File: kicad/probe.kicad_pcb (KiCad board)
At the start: 2 copper layers, 22 parts, among them IC1 ATTINY85, IC2 MAX7219, P1 ICSP, P2 5V

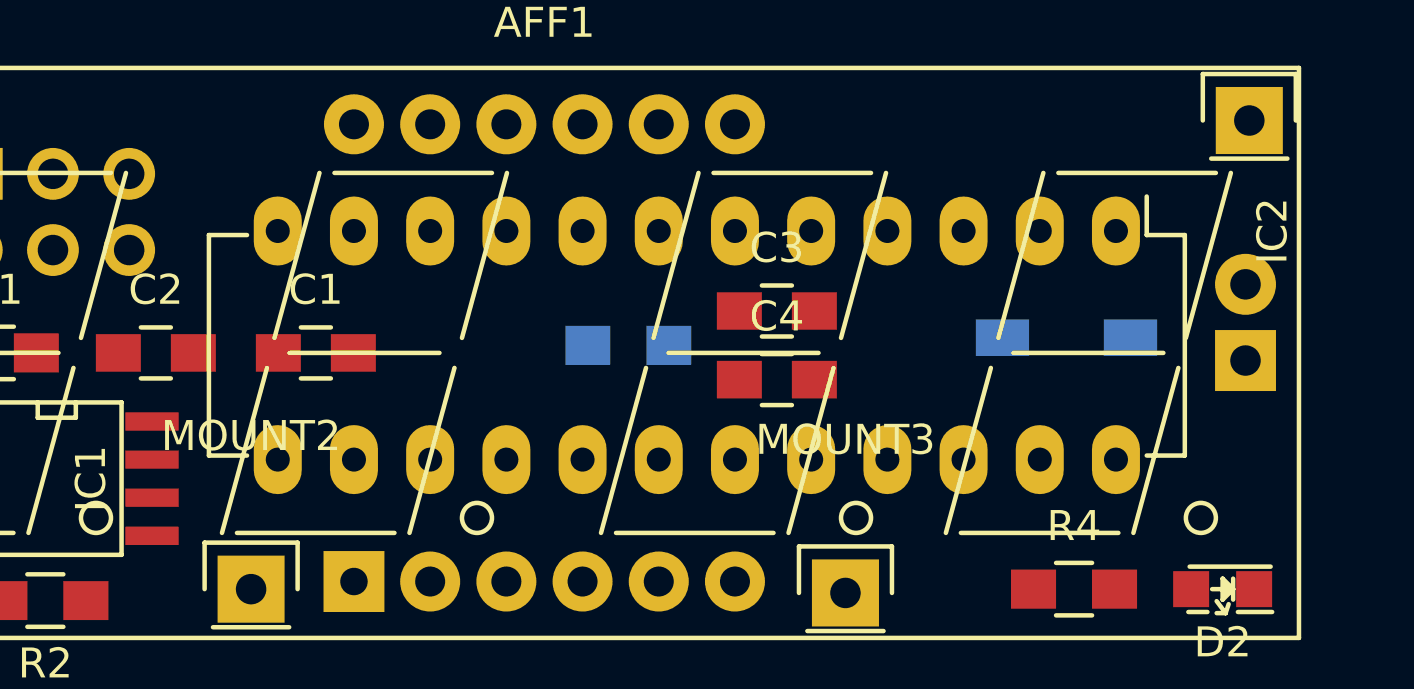
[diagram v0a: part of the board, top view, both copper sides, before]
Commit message: Drawing of the real display dimensions
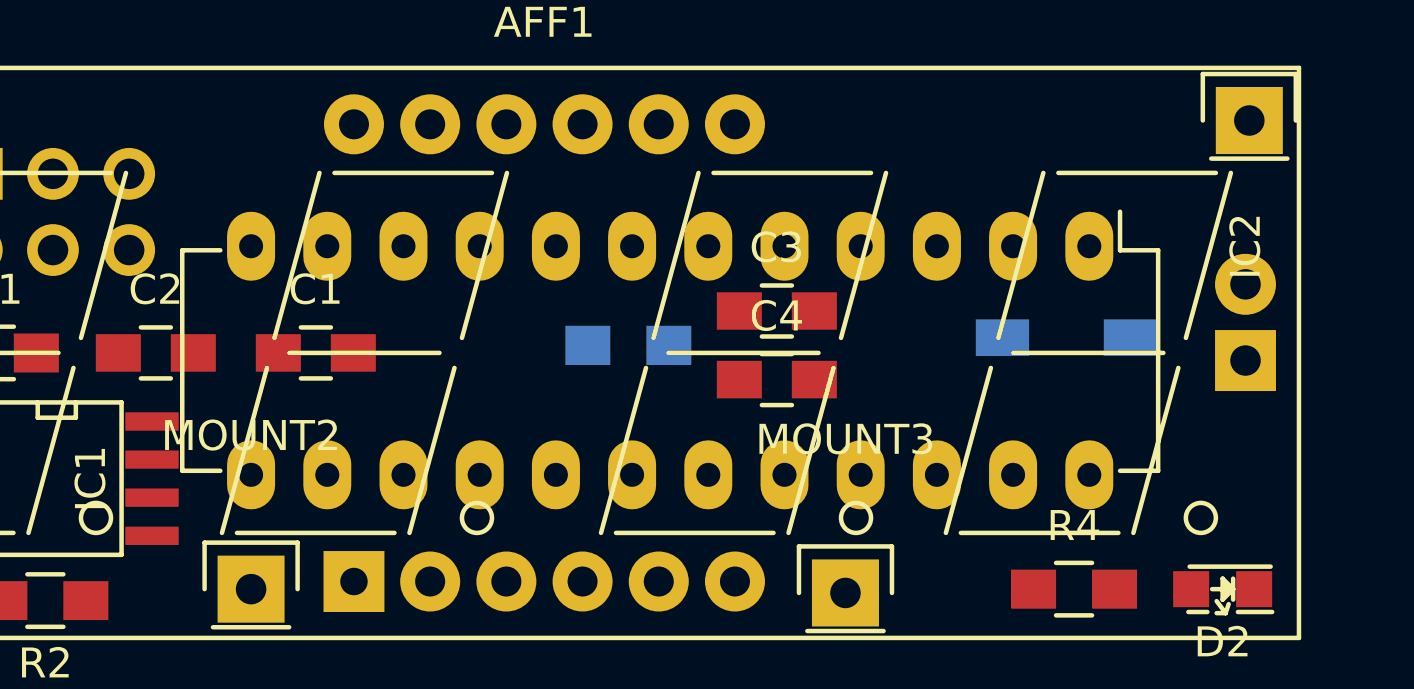
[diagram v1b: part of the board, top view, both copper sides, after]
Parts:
- moved IC2 1.02 mm to (175.3, 78.7)
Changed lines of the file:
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@@
-(kicad_pcb (version 4) (host pcbnew 4.0.2-stable)
+(kicad_pcb (version 4) (host pcbnew 4.0.4+e1-6308~48~ubuntu16.04.1-stable)
   (general
     (links 53)
     (no_connects 53)
-    (area 97.936267 55.1636 219.436734 121.434401)
+    (area 128.491267 68.0136 185.833734 94.5774)
     (thickness 1.6)
-    (drawings 0)
+    (drawings 3)
     (tracks 0)
     (zones 0)
@@
   )
   (module Housings_DIP:DIP-24_W7.62mm_LongPads (layer F.Cu)
-    (at 176.149 78.232 270)
+    (at 175.26 78.74 270)
     (descr "24-lead dip package, row spacing 7.62 mm (300 mils), longer pads")
     (tags "dil dip 2.54 300")
@@
     )
   )
+  (dimension 30.48 (width 0.3) (layer Dwgs.User)
+    (gr_text "30.480 mm" (at 172.72 130.89) (layer Dwgs.User)
+      (effects (font (size 1.5 1.5) (thickness 0.3)))
+    )
+    (feature1 (pts (xy 157.48 121.92) (xy 157.48 132.24)))
+    (feature2 (pts (xy 187.96 121.92) (xy 187.96 132.24)))
+    (crossbar (pts (xy 187.96 129.54) (xy 157.48 129.54)))
+    (arrow1a (pts (xy 157.48 129.54) (xy 158.606504 128.953579)))
+    (arrow1b (pts (xy 157.48 129.54) (xy 158.606504 130.126421)))
+    (arrow2a (pts (xy 187.96 129.54) (xy 186.833496 128.953579)))
+    (arrow2b (pts (xy 187.96 129.54) (xy 186.833496 130.126421)))
+  )
+  (dimension 15.24 (width 0.3) (layer Dwgs.User)
+    (gr_text "15.240 mm" (at 194.39 109.22 270) (layer Dwgs.User)
+      (effects (font (size 1.5 1.5) (thickness 0.3)))
+    )
+    (feature1 (pts (xy 187.96 116.84) (xy 195.74 116.84)))
+    (feature2 (pts (xy 187.96 101.6) (xy 195.74 101.6)))
+    (crossbar (pts (xy 193.04 101.6) (xy 193.04 116.84)))
+    (arrow1a (pts (xy 193.04 116.84) (xy 192.453579 115.713496)))
+    (arrow1b (pts (xy 193.04 116.84) (xy 193.626421 115.713496)))
+    (arrow2a (pts (xy 193.04 101.6) (xy 192.453579 102.726504)))
+    (arrow2b (pts (xy 193.04 101.6) (xy 193.626421 102.726504)))
+  )
+  (dimension 17.78 (width 0.3) (layer Dwgs.User)
+    (gr_text "17.780 mm" (at 204.55 82.55 270) (layer Dwgs.User)
+      (effects (font (size 1.5 1.5) (thickness 0.3)))
+    )
+    (feature1 (pts (xy 187.96 91.44) (xy 205.9 91.44)))
+    (feature2 (pts (xy 187.96 73.66) (xy 205.9 73.66)))
+    (crossbar (pts (xy 203.2 73.66) (xy 203.2 91.44)))
+    (arrow1a (pts (xy 203.2 91.44) (xy 202.613579 90.313496)))
+    (arrow1b (pts (xy 203.2 91.44) (xy 203.786421 90.313496)))
+    (arrow2a (pts (xy 203.2 73.66) (xy 202.613579 74.786504)))
+    (arrow2b (pts (xy 203.2 73.66) (xy 203.786421 74.786504)))
+  )
 )

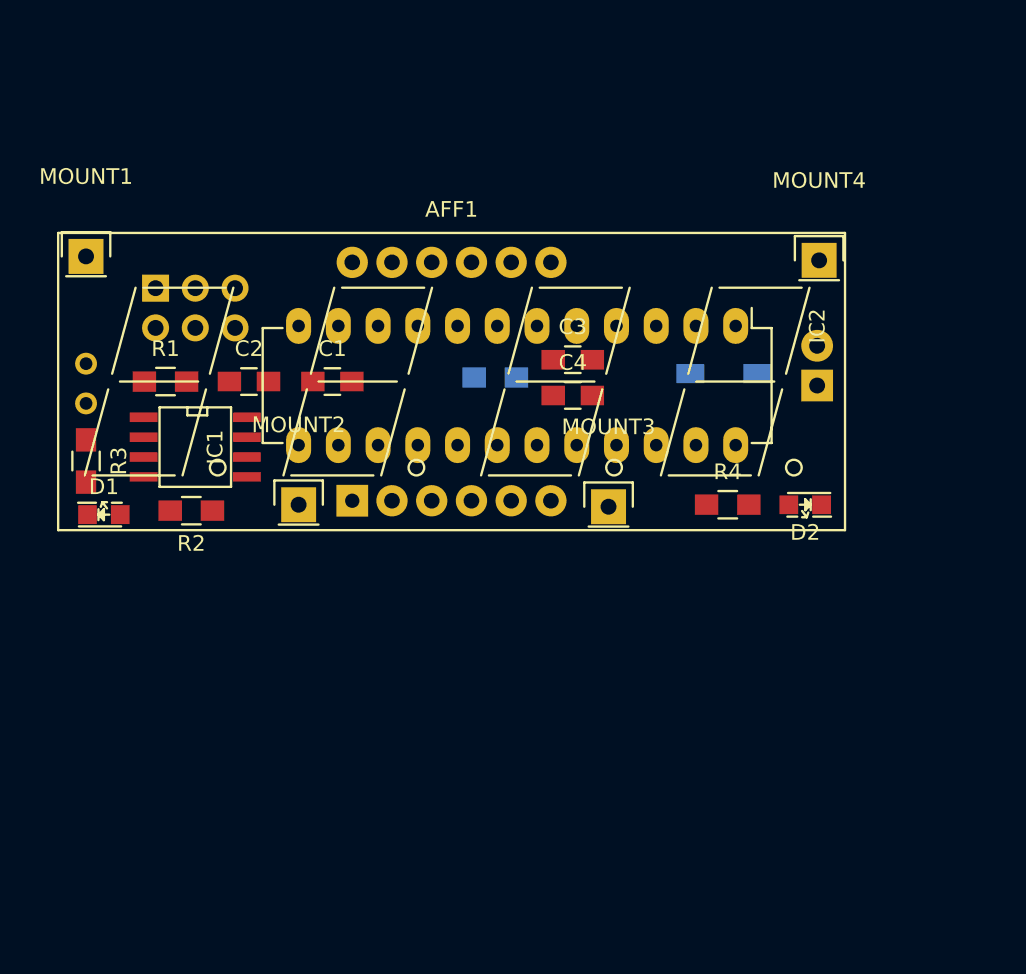
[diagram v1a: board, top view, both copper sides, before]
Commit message: New layout with correct size display
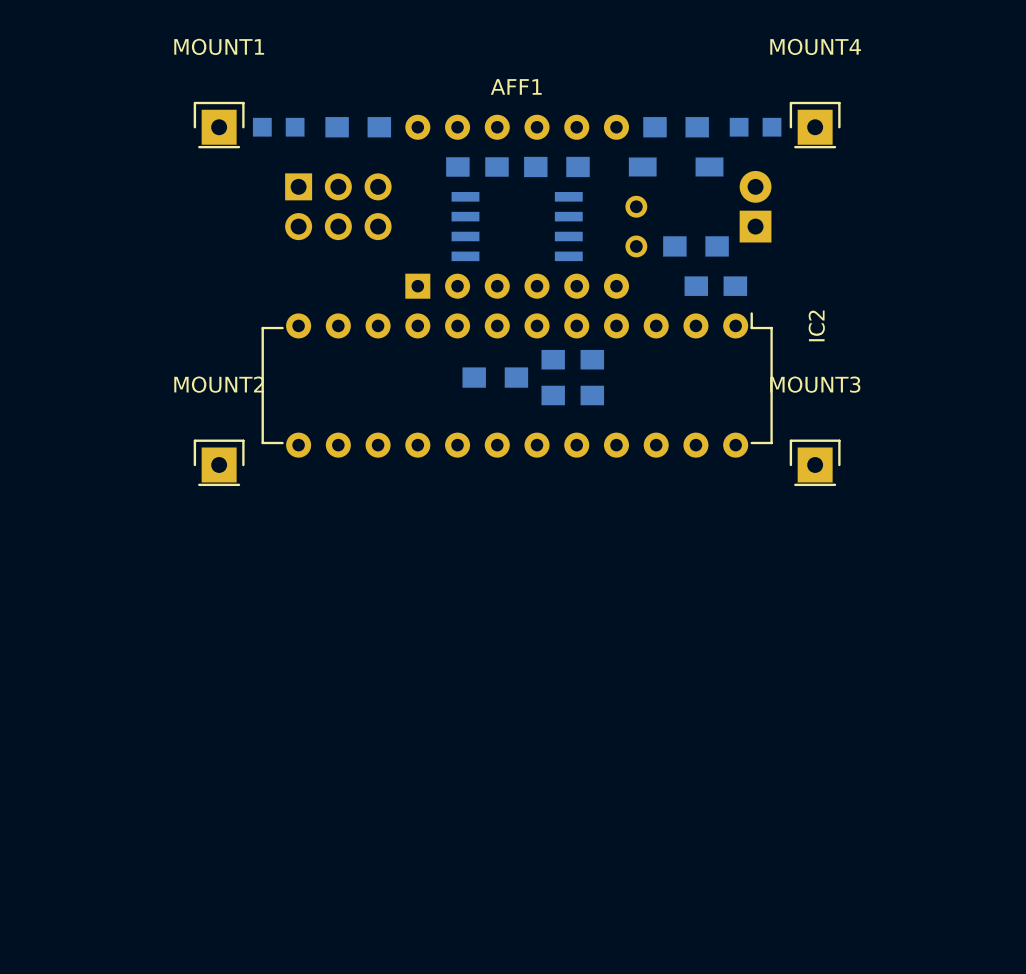
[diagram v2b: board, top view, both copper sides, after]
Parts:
- AFF1: footprint Displays_7-Segment:Cx56-12 -> 4x7seg_CA
- C1, C2, C3, C4, D1, D2, IC1, R1, R2, R3, R4: moved to B.Cu
- IC2: footprint Housings_DIP:DIP-24_W7.62mm_LongPads -> Housings_DIP:DIP-24_W7.62mm
- moved R3 41.3 mm to (172.7, 73.7), turned to 0 degrees
- moved TH1 36.6 mm to (168.9, 72.4)
- moved R1 28.5 mm to (163.8, 68.6)
- moved D1 27.2 mm to (146.1, 66.0)
- moved R2 26.7 mm to (151.1, 66.0)
- moved C1 25.3 mm to (174.0, 76.2)
- moved IC1 24.9 mm to (161.3, 72.4)
- moved R4 24.4 mm to (171.4, 66.0)
- moved D2 24.3 mm to (176.5, 66.0)
- moved C2 20.0 mm to (158.8, 68.6)
- moved AFF1 14.3 mm to (154.9, 76.2)
- moved D3 13.6 mm to (171.4, 68.6)
- moved MOUNT3 13.5 mm to (180.3, 87.6)
- moved MOUNT1 11.9 mm to (142.2, 66.0)
- moved P1 11.2 mm to (147.3, 69.8)
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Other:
- board text added: "+"
- board text added: "-"
- board text added: "MISO"
- board text added: "RST"

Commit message: 2 displays & 2 thermistors on perfboard
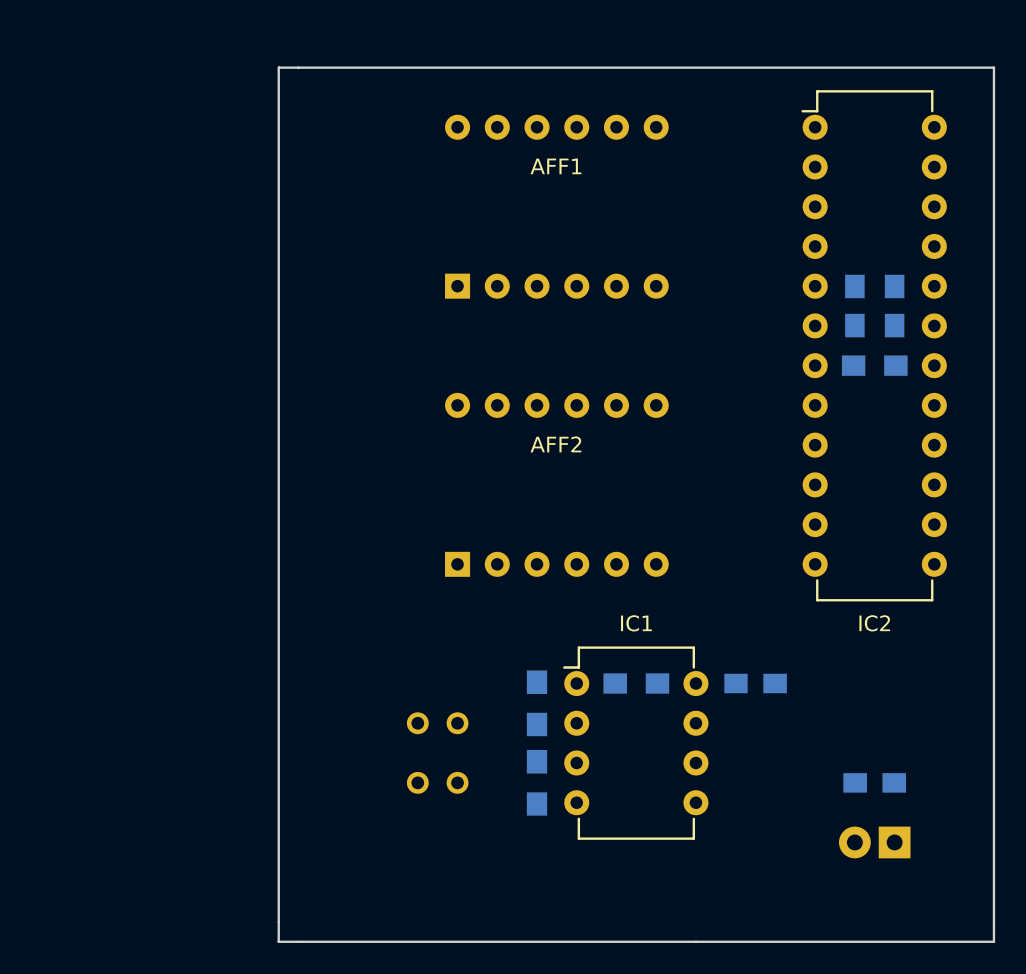
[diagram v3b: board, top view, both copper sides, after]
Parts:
- removed D1: Led, theapi_footprints:LED_0805
- removed D2: LED, theapi_footprints:LED_0805
- removed D3: D_Schottky, theapi_footprints:SOD-123-Schottky
- removed MOUNT1, MOUNT2, MOUNT3, MOUNT4: CONN_01X01, Pin_Headers:Pin_Header_Straight_1x01
- removed P1: ICSP, Pin_Headers:Pin_Header_Straight_2x03
- removed R4: R, Resistors_SMD:R_0805_HandSoldering
- added AFF2: CC56-12, theapi_footprints:4x7seg_CA, F.Cu at (157.5, 94.0)
- added TH2: THERMISTOR, Discret:R1, B.Cu at (156.2, 108.0)
- AFF1: footprint 4x7seg_CA -> theapi_footprints:4x7seg_CA
- IC1: footprint theapi_footprints:SOIC-8-N-handsolder -> Housings_DIP:DIP-8_W7.62mm; moved to F.Cu
- R2: value 820 -> R
- moved R2 43.4 mm to (162.6, 108.0), turned to 270 degrees
- moved P2 40.4 mm to (185.4, 111.8), turned to 90 degrees
- moved C2 37.5 mm to (176.5, 101.6)
- moved TH1 34.2 mm to (156.2, 104.1), turned to 0 degrees
- moved R1 33.4 mm to (168.9, 101.6)
- moved C1 33.3 mm to (184.2, 108.0)
- moved R3 30.9 mm to (162.6, 102.9), turned to 90 degrees
- moved IC1 29.5 mm to (165.1, 101.6), turned to 0 degrees
- moved 33K1 24.3 mm to (184.2, 81.3), turned to 180 degrees
- moved C4 21.4 mm to (185.4, 77.5), turned to 90 degrees
- moved C3 18.4 mm to (182.9, 77.5), turned to 90 degrees
- moved IC2 13.7 mm to (180.3, 66.0), turned to 0 degrees
- moved AFF1 2.54 mm to (157.5, 76.2)
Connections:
- IC1 pad 3: /PB4 -> /ADC2
- IC2 pad 12: /PB4 -> /MISO
- P2 pad 2: Net-(D3-Pad2) -> /VCC
- R2 pad 1: /MISO -> /ADC2
- R2 pad 2: Net-(D1-Pad2) -> GND
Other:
- board outline added: 45.7 x 55.9 mm
- board text removed: "+"
- board text removed: "-"
- board text removed: "MISO"
- board text removed: "RST"

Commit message: Initial routing
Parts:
- moved TH1 2.84 mm to (157.5, 101.6)
- moved TH2 2.84 mm to (157.5, 110.5)
- moved C3 2.56 mm to (182.9, 74.9)
- moved C4 2.56 mm to (185.4, 74.9)
- moved R3 1.89 mm to (161.3, 104.3), turned to 180 degrees
- moved R2 1.85 mm to (161.2, 106.7), turned to 180 degrees
- moved 33K1 1.80 mm to (185.4, 80.0), turned to 90 degrees
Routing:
- net GND: track 0.00 -> 130.8 mm
- net /VCC: track 0.00 -> 110.6 mm
- net /MOSI: track 0.00 -> 79.8 mm
- net Net-(AFF1-Pad2): track 0.00 -> 79.6 mm
- net Net-(AFF1-Pad3): track 0.00 -> 73.0 mm
- net Net-(AFF1-Pad1): track 0.00 -> 66.4 mm
- net Net-(AFF1-Pad4): track 0.00 -> 63.1 mm
- net Net-(AFF2-Pad12): track 0.00 -> 52.3 mm
- net Net-(AFF1-Pad11): track 0.00 -> 50.9 mm
- net Net-(AFF1-Pad10): track 0.00 -> 48.0 mm
- net Net-(AFF1-Pad5): track 0.00 -> 46.9 mm
- net Net-(AFF2-Pad8): track 0.00 -> 38.9 mm
- net Net-(AFF1-Pad7): track 0.00 -> 38.7 mm
- net Net-(AFF1-Pad9): track 0.00 -> 34.5 mm
- net Net-(AFF1-Pad12): track 0.00 -> 25.7 mm
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
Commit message: Layout tweek
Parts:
- added REF**: TheApiLogoTiny, theapi_footprints:TheApiLogoTiny, F.Cu at (183.8, 102.2)
- R2, R3: moved to F.Cu
- moved R3 3.81 mm to (157.5, 104.1)
- moved R2 3.73 mm to (157.5, 106.7)
- moved C3 2.56 mm to (183.0, 77.5)
- moved C4 2.56 mm to (185.5, 77.5)
- moved 33K1 1.71 mm to (184.3, 81.3), turned to 180 degrees
- moved TH2 1.27 mm to (157.5, 109.2)
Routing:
- net Net-(AFF2-Pad8): track 38.9 -> 15.9 mm
- net GND: track 130.8 -> 120.0 mm, vias 0 -> 3
- net /VCC: track 110.6 -> 101.9 mm
- net Net-(AFF2-Pad12): track 52.3 -> 43.7 mm
- net Net-(AFF1-Pad9): track 34.5 -> 42.7 mm
- net Net-(AFF1-Pad8): track 19.6 -> 27.5 mm
- net /SCK: track 19.4 -> 26.0 mm
- net /MOSI: track 79.8 -> 84.1 mm
- net /MISO: track 17.9 -> 21.5 mm
- net Net-(AFF2-Pad6): track 15.0 -> 17.6 mm
- net Net-(AFF1-Pad1): track 66.4 -> 68.3 mm
- net Net-(AFF1-Pad4): track 63.1 -> 64.5 mm
- net Net-(AFF1-Pad11): track 50.9 -> 51.9 mm
- net /ADC2: track 7.93 -> 8.84 mm
- net Net-(AFF1-Pad2): track 79.6 -> 80.3 mm
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- added copper zone on B.Cu, net GND
- added copper zone on F.Cu, net GND
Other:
- net class Wide: trace_width 0.3048 -> 0.8128

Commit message: Better accuracy
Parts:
- moved R2 6.35 mm to (152.4, 110.5), turned to 0 degrees
- moved R3 5.24 mm to (152.4, 105.4), turned to 0 degrees
- moved TH1 1.27 mm to (157.5, 102.9), turned to 180 degrees
- moved TH2 1.27 mm to (157.5, 108.0), turned to 180 degrees
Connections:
- R2 pad 1: /ADC2 -> /VCC
- R2 pad 2: GND -> /ADC2
- R3 pad 1: /ADC3 -> /VCC
- R3 pad 2: GND -> /ADC3
- TH1 pad 1: /VCC -> /ADC3
- TH1 pad 2: /ADC3 -> GND
- TH2 pad 1: /VCC -> /ADC2
- TH2 pad 2: /ADC2 -> GND
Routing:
- net /VCC: track 101.9 -> 121.6 mm
- net GND: track 120.0 -> 115.1 mm
- net /ADC2: track 8.84 -> 12.9 mm
- net /ADC3: track 8.84 -> 12.9 mm
